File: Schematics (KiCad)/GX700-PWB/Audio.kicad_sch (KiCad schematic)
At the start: 10 parts, among them CN12 B4PSHF1AA, CN19 B5PSHF1AA

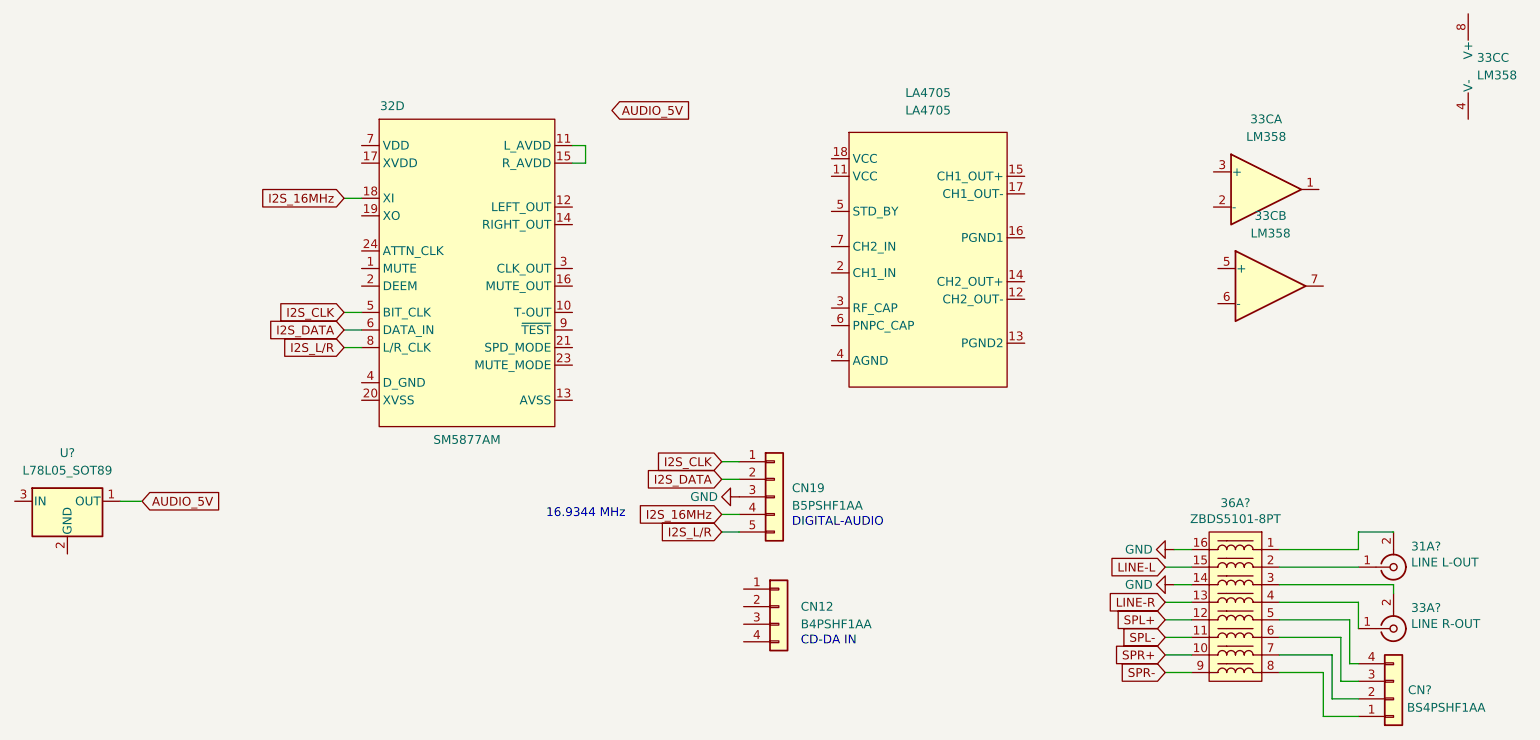
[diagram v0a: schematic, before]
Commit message: Added Symbols, PSX page
Added PSX CPU and GPU symbols, added a COH PSX skeleton schematic and also updated the JAMMA symbol and footprint as it was bad.
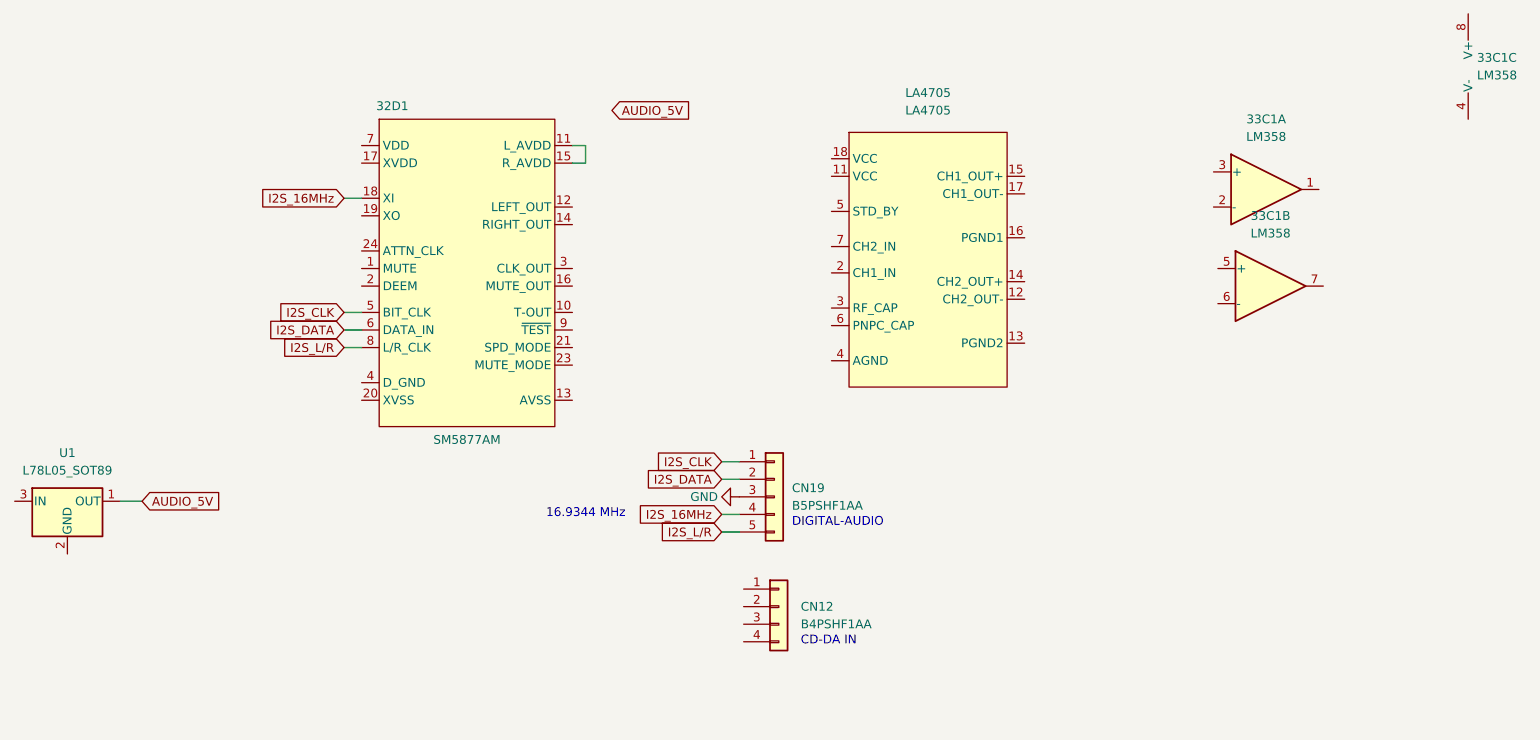
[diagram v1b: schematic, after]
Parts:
- removed 31A?: LINE L-OUT, symbol Connector:Conn_Coaxial
- removed 33A?: LINE R-OUT, symbol Connector:Conn_Coaxial
- removed 36A?: ZBDS5101-8PT, Package_SO:SOIC-16_4.55x10.3mm_P1.27mm, symbol Ksys573-rescue:ZBDS5101-8PT-Filter
- removed CN?: BS4PSHF1AA, symbol Connector_Generic:Conn_01x04
- gave numbers to parts that had none: 1
- renumbered 32D to 32D1, 33C to 33C1

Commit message: Major board changes to give a rough render of the PCB
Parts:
- LA4705: footprint Package_SIP:SIP18_Housing -> Connector_PinHeader_2.00mm:PinHeader_1x18_P2.00mm_Vertical
